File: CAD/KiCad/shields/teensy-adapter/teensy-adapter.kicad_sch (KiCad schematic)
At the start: 0 parts

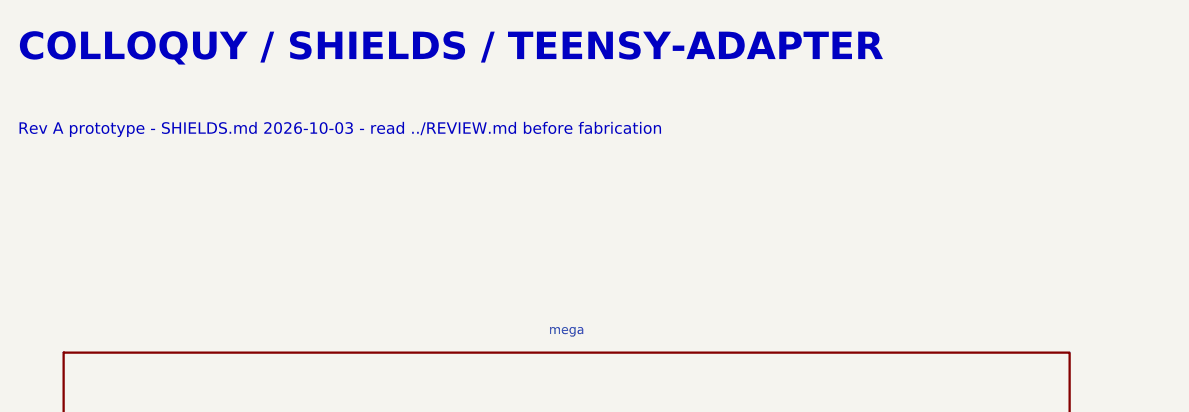
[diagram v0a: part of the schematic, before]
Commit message: Remove shield identification and adopt the simplified connector and Teensy pin maps
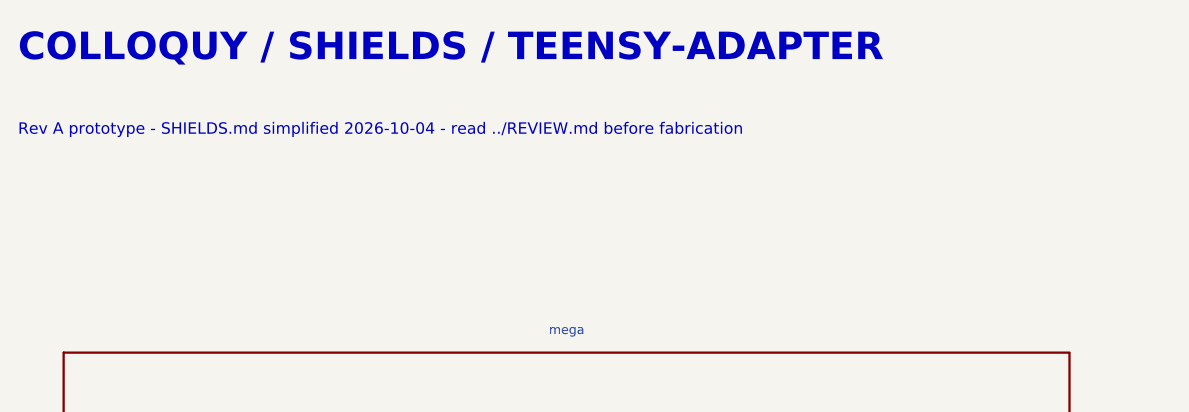
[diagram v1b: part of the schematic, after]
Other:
- note added: "Rev A prototype - SHIELDS.md simplified 2026-10-04 - read ../REVIEW.md before fabrication"
- note removed: "Rev A prototype - SHIELDS.md 2026-10-03 - read ../REVIEW.md before fabrication"

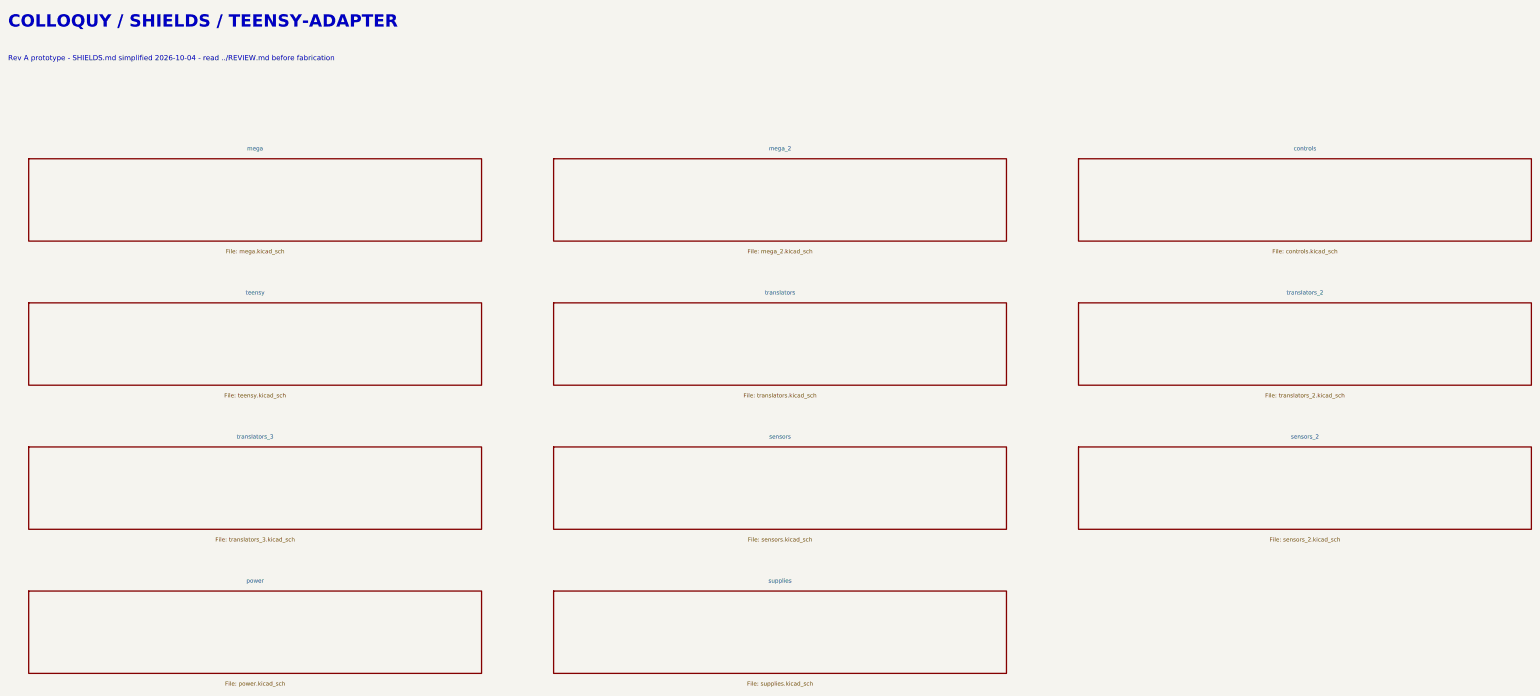
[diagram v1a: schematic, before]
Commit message: Route microphones directly to Teensy and remove the analyser buffer board
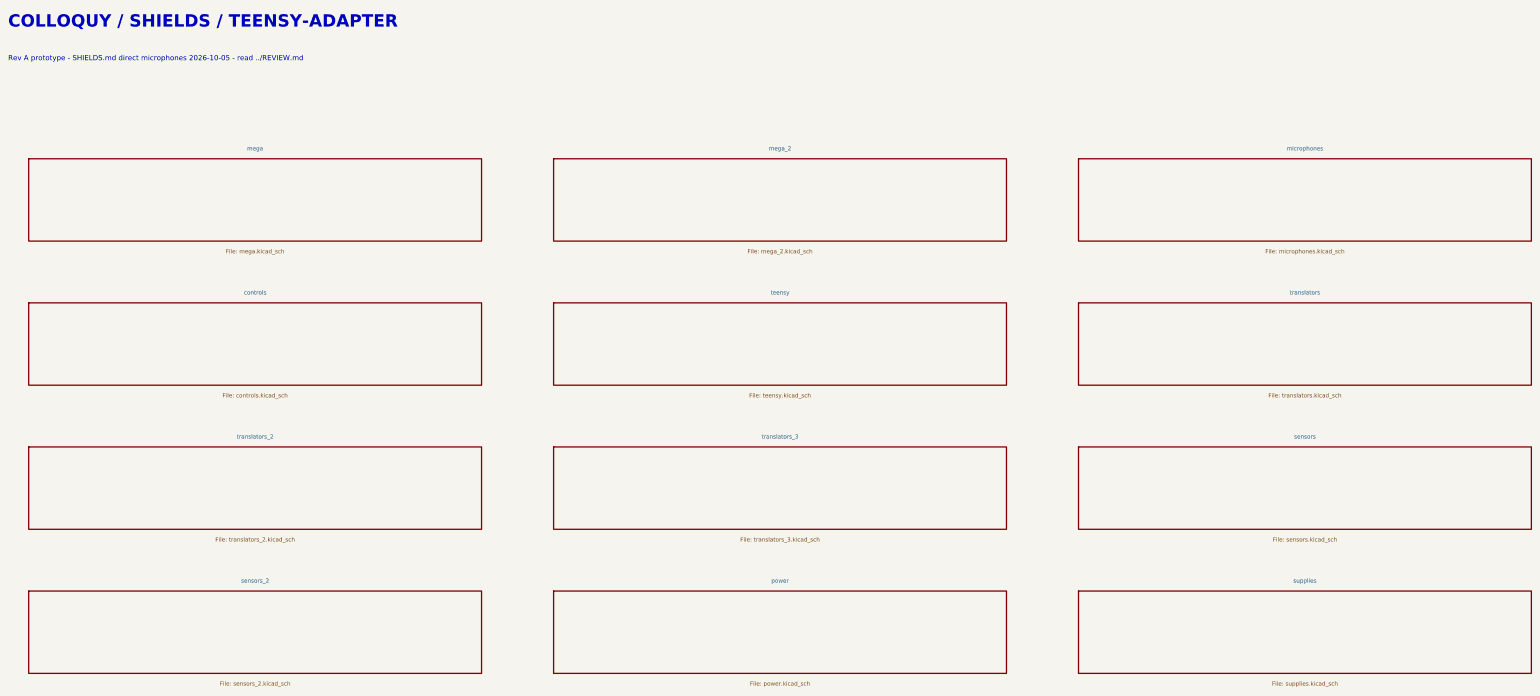
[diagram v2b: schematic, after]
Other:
- added sheet microphones (microphones.kicad_sch)
- note added: "Rev A prototype - SHIELDS.md direct microphones 2026-10-05 - read ../REVIEW.md"
- note removed: "Rev A prototype - SHIELDS.md simplified 2026-10-04 - read ../REVIEW.md before fabrication"
